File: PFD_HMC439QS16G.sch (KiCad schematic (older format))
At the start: 42 parts, among them J1 REF, J2 IN, J3 Out, J4 Supply, U1 HMC439QS16G, U2 LT3045EMSE, U3 LT3094EMSE, U4 ADA4896-2ARMZ

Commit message: Rev 1.1
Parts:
- added C20: 560p, Capacitor_SMD:C_0603_1608Metric, symbol Device:C_Small
- added C21, C22: 100n, Capacitor_SMD:C_0603_1608Metric, symbol Device:C_Small
- added C23: 33p, Capacitor_SMD:C_0603_1608Metric, symbol Device:C_Small
- added C24: 330p, Capacitor_SMD:C_0603_1608Metric, symbol Device:C_Small
- added H1, H2, H3, H4: MountingHole_Pad, MountingHole:MountingHole_4.3mm_M4_Pad_Via, symbol Mechanical:MountingHole_Pad
- added J5: JFET/Bias-T, Connector_Coaxial:SMA_Amphenol_901-144_Vertical, symbol Connector:Conn_Coaxial
- added JP1: Inverting, Jumper:SolderJumper-2_P1.3mm_Open_RoundedPad1.0x1.5mm, symbol Device:Jumper_NO_Small
- added JP2: Non-Inverting, Jumper:SolderJumper-2_P1.3mm_Open_RoundedPad1.0x1.5mm, symbol Device:Jumper_NO_Small
- added LOGO1: Logo_APQ, footprints:APQ-Logo, symbol Custom_logos:Logo_APQ
- added LOGO2: Logo_Open_Hardware_Small, Symbol:OSHW-Logo_5.7x6mm_SilkScreen, symbol Graphic:Logo_Open_Hardware_Small
- added LOGO3: Logo_ROHS, Symbol:RoHS-Logo_6mm_SilkScreen, symbol Custom_logos:Logo_ROHS
- added R16, R17, R18: 200, Resistor_SMD:R_0603_1608Metric, symbol Device:R_Small
- added R19: 51, Resistor_SMD:R_1210_3225Metric, symbol Device:R_Small
- added R20: 1.2k, Resistor_SMD:R_0603_1608Metric, symbol Device:R_Small
- added R21: 51, Resistor_SMD:R_0603_1608Metric, symbol Device:R_Small
- added RV1: 1k, Potentiometer_THT:Potentiometer_Vishay_43_Horizontal, symbol Device:R_POT_TRIM
- added U5: ADA4896-2ARMZ, footprints:MSOP-8_3x3mm_P0.65mm_mod, symbol Linear-Technology:ADA4896-2ARMZ
- C1, C2: footprint Capacitors_SMD:C_0402 -> Capacitor_SMD:C_0402_1005Metric
- C10, C15, C16, C17, C18, C19, C5, C6, C9: footprint Capacitors_SMD:C_0603 -> Capacitor_SMD:C_0603_1608Metric
- C11, C12, C3, C4: footprint Capacitors_SMD:C_1210 -> Capacitor_SMD:C_1210_3225Metric
- C13, C14: value 200p -> 33p; footprint Capacitors_SMD:C_0603 -> Capacitor_SMD:C_0603_1608Metric
- C7: footprint Capacitors_SMD:C_1206 -> Capacitor_SMD:C_1206_3216Metric
- C8: value 4.7u -> 0.47u; footprint Capacitors_SMD:C_1206 -> Capacitor_SMD:C_1206_3216Metric
- J1, J2: footprint Connectors:SMA_THT_Jack_Straight -> Connector_Coaxial:SMA_Amphenol_901-144_Vertical; symbol PFD_HMC439QS16G-rescue:CONN_01X02 -> Connector:Conn_Coaxial
- J3: value Out -> Error_Out; footprint Connectors:SMA_THT_Jack_Straight -> Connector_Coaxial:SMA_Amphenol_901-144_Vertical; symbol PFD_HMC439QS16G-rescue:CONN_01X02 -> Connector:Conn_Coaxial
- J4: footprint Pin_Headers:Pin_Header_Straight_1x03_Pitch2.54mm -> Connector_PinHeader_2.54mm:PinHeader_1x03_P2.54mm_Vertical; symbol PFD_HMC439QS16G-rescue:CONN_01X03 -> Connector_Generic:Conn_01x03
- R1, R10, R11, R12, R13, R14, R2, R3, R4, R5, R6, R7, R8, R9: footprint Resistors_SMD:R_0603 -> Resistor_SMD:R_0603_1608Metric
- R15: footprint Resistors_SMD:R_1210 -> Resistor_SMD:R_1210_3225Metric
- U1: footprint custom:QSOP-16_EP_3.9x4.9mm_Pitch0.635mm -> footprints:QSOP-16_3.9x4.9mm_P0.635mm_EP_2.3mmx1.75mm
- U2, U3: footprint Housings_SSOP:MSOP-12-1EP_3x4mm_Pitch0.65mm -> Package_SO:MSOP-12-1EP_3x4mm_P0.65mm_EP1.65x2.85mm
- U4: footprint Housings_SSOP:MSOP-8_3x3mm_Pitch0.65mm -> footprints:MSOP-8_3x3mm_P0.65mm_mod
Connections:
- wire segments 156 -> 210
- no-connect marks 0 -> 6
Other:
- note added: "Fixed Pi attenuator: 34 dB\n(reduce attenuation if \na larger 'gain' is required)"
- note added: "Non-inverting option:\nJP1: open, JP2: closed, R17: 200\n\nInverting option:\nJP1: closed, JP2: open, R17: DNF\n\n(Note, that U4B and U4A are inverting)"
- moved on the sheet: C1, C10, C11, C12, C13, C14, C15, C16, C17, C18, C19, C2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

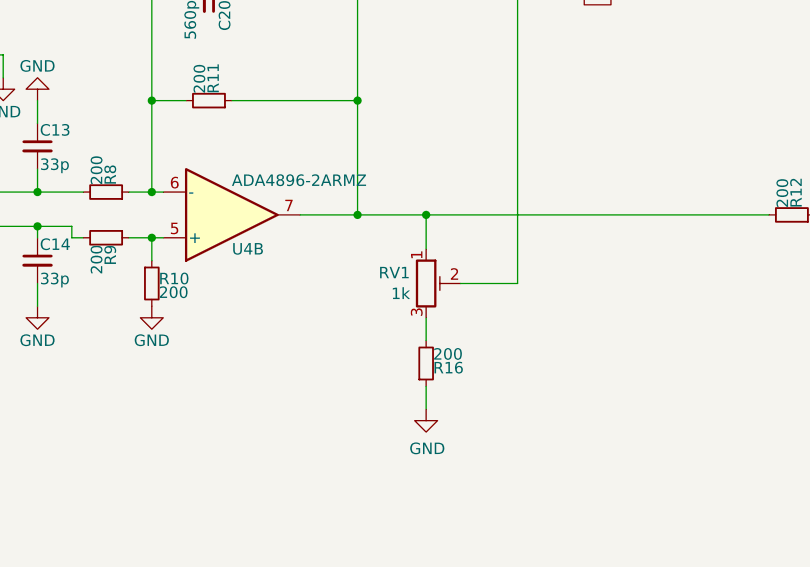
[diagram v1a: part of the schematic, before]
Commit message: Reverse Trimpot. Update gerber files
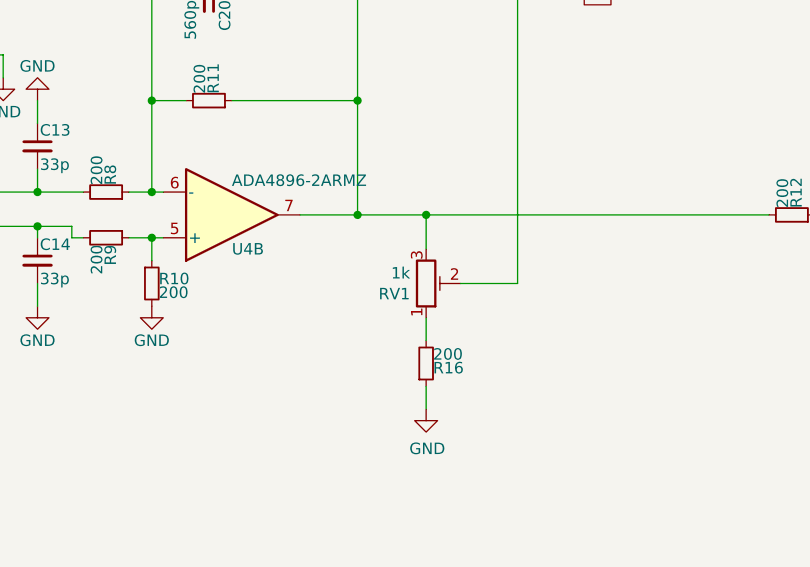
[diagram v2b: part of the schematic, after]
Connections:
- net at C20.1, R11.1, R12.2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: now also RV1.3; no longer RV1.1
- net at R16.2: now also RV1.1; no longer RV1.3
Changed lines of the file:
@@
 F 3 "~" H 6600 4050 50  0001 C CNN
 	1    6600 4050
-	1    0    0    -1
+	1    0    0    1
 $EndComp
 $Comp

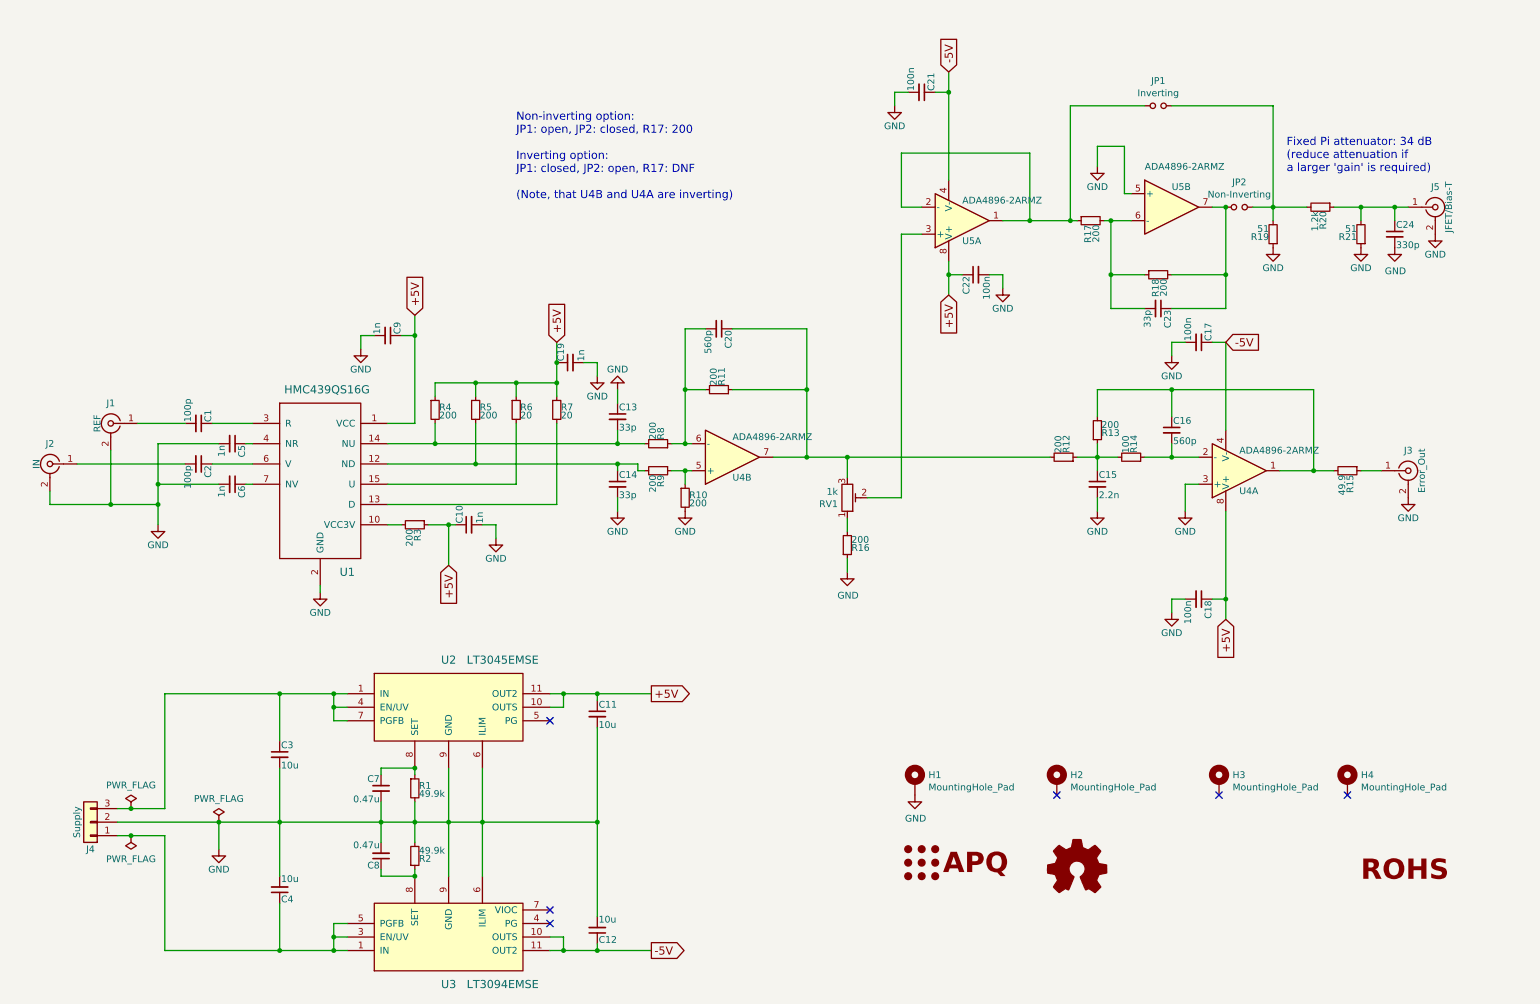
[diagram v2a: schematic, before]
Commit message: Rev. 1.2
-Divide input signal by 4 using HMC365
-Change board layout to standard eurocard
-Minor changes to 'Fast Out': Optional AC-coupling, optional gain
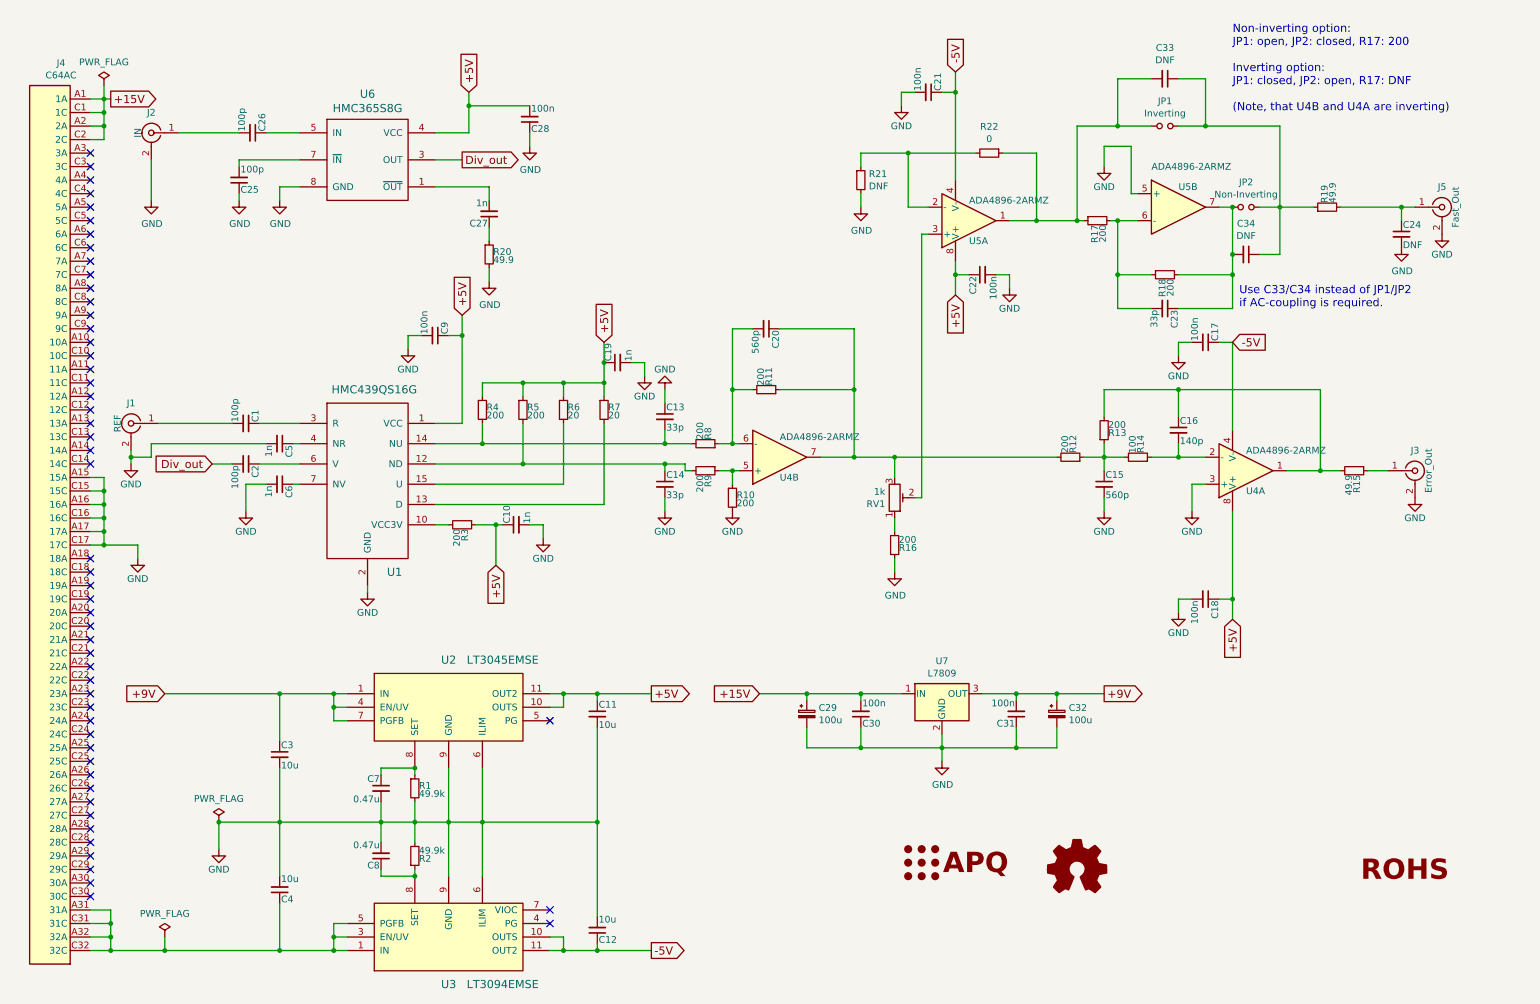
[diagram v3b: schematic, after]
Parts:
- removed H1, H2, H3, H4: MountingHole_Pad, MountingHole:MountingHole_4.3mm_M4_Pad_Via, symbol Mechanical:MountingHole_Pad
- removed J4: Supply, Connector_PinHeader_2.54mm:PinHeader_1x03_P2.54mm_Vertical, symbol Connector_Generic:Conn_01x03
- added C25, C26: 100p, Capacitor_SMD:C_0402_1005Metric, symbol Device:C_Small
- added C27: 1n, Capacitor_SMD:C_0603_1608Metric, symbol Device:C_Small
- added C28, C30, C31: 100n, Capacitor_SMD:C_0603_1608Metric, symbol Device:C_Small
- added C29, C32: 100u, Capacitor_THT:CP_Radial_D5.0mm_P2.50mm, symbol Device:CP_Small
- added C33, C34: DNF, Capacitor_THT:C_Rect_L7.2mm_W3.0mm_P5.00mm_FKS2_FKP2_MKS2_MKP2, symbol Device:C_Small
- added J4: C64AC, footprints:Socket_DIN41612-CaseC1-AC-Male-64Pin-2rows, symbol Connector:C64AC
- added R22: 0, Capacitor_SMD:C_0603_1608Metric, symbol Device:R_Small
- added U6: HMC365S8G, Package_SO:SOIC-8-1EP_3.9x4.9mm_P1.27mm_EP2.41x3.81mm, symbol Linear-Technology:HMC365S8G
- added U7: L7809, Package_TO_SOT_THT:TO-220-3_Vertical, symbol Regulator_Linear:L7809
- C15: value 2.2n -> 560p
- C16: value 560p -> 140p
- C24: value 330p -> DNF
- C9: value 1n -> 100n
- J3: footprint Connector_Coaxial:SMA_Amphenol_901-144_Vertical -> Connector_Coaxial:BNC_Amphenol_B6252HB-NPP3G-50_Horizontal
- J5: value JFET/Bias-T -> Fast_Out; footprint Connector_Coaxial:SMA_Amphenol_901-144_Vertical -> Connector_Coaxial:BNC_Amphenol_B6252HB-NPP3G-50_Horizontal
- R19: value 51 -> 49.9
- R20: value 1.2k -> 49.9
- R21: value 51 -> DNF; footprint Resistor_SMD:R_0603_1608Metric -> Capacitor_SMD:C_0603_1608Metric
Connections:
- net +5V: now also C28.2, U6.4 (VCC)
- net GND: now also R20.2, R21.2, C25.1, C28.1, C29.2, C30.1, C31.1, C32.2, J4.A15 (15A), J4.A16 (16A), J4.A17 (17A), J4.C15 (15C), J4.C16 (16C), J4.C17 (17C), U6.8 (GND), U6.9 (GND), U7.2 (GND); no longer R19.1, R21.1
- net IN: now also J4.A31 (31A), J4.A32 (32A), J4.C31 (31C), J4.C32 (32C)
- net IN2: now also C31.2, C32.1, U7.3 (OUT)
- net at J2.1 (In): now also C26.2; no longer C2.2
- net at C24.1, J5.1 (In): now also R19.2; no longer R20.1, R21.2
- net at JP1.2, JP2.2: now also R19.1, C33.1, C34.1; no longer R19.2, R20.2
- net at JP1.1, R17.1, U5.1: now also C33.2, R22.1; no longer U5.2 (-)
- net at C23.1, JP2.1, R18.2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: now also C34.2
- new net: R21.1, R22.2, U5.2 (-)
- new net: C27.2, U6.1 (~OUT~)
- new net: C26.1, U6.5 (IN)
- new net: C25.2, U6.7 (~IN~)
- new net: C27.1, R20.1
- new net +15V: C29.1, C30.2, J4.A1 (1A), J4.A2 (2A), J4.C1 (1C), J4.C2 (2C), U7.1 (IN)
- new net Div_out: C2.2, U6.3 (OUT)
- no-connect marks 6 -> 53
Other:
- note added: "Use C33/C34 instead of JP1/JP2\nif AC-coupling is required."
- note removed: "Fixed Pi attenuator: 34 dB\n(reduce attenuation if \na larger 'gain' is required)"
- moved on the sheet: C1, C10, C13, C14, C15, C16, C17, C18, C19, C2, C20, C21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

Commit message: Add gain of 2 and increase bandwidth at U4B
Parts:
- C20: value 560p -> 15p
- R10, R11: value 200 -> 380
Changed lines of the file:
@@
 P 5750 4050
 F 0 "R10" H 5780 4070 50  0000 L CNN
-F 1 "200" H 5780 4010 50  0000 L CNN
+F 1 "380" H 5780 4010 50  0000 L CNN
 F 2 "Resistor_SMD:R_0603_1608Metric" H 5750 4050 50  0001 C CNN
 F 3 "" H 5750 4050 50  0001 C CNN
@@
 P 6000 3250
 F 0 "R11" H 6030 3270 50  0000 L CNN
-F 1 "200" H 6030 3210 50  0000 L CNN
+F 1 "380" H 6030 3210 50  0000 L CNN
 F 2 "Resistor_SMD:R_0603_1608Metric" H 6000 3250 50  0001 C CNN
 F 3 "" H 6000 3250 50  0001 C CNN
@@
 P 6000 2800
 F 0 "C20" H 6010 2870 50  0000 L CNN
-F 1 "560p" H 6010 2720 50  0000 L CNN
+F 1 "15p" H 6010 2720 50  0000 L CNN
 F 2 "Capacitor_SMD:C_0603_1608Metric" H 6000 2800 50  0001 C CNN
 F 3 "" H 6000 2800 50  0001 C CNN

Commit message: First draft: fast PD regulator
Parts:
- removed C21, C22: 100n, Capacitor_SMD:C_0603_1608Metric, symbol Device:C_Small
- removed C23: 33p, Capacitor_SMD:C_0603_1608Metric, symbol Device:C_Small
- removed C24: DNF, Capacitor_SMD:C_0603_1608Metric, symbol Device:C_Small
- removed C33, C34: DNF, Capacitor_THT:C_Rect_L7.2mm_W3.0mm_P5.00mm_FKS2_FKP2_MKS2_MKP2, symbol Device:C_Small
- removed J5: Fast_Out, Connector_Coaxial:BNC_Amphenol_B6252HB-NPP3G-50_Horizontal, symbol Connector:Conn_Coaxial
- removed JP1: Inverting, Jumper:SolderJumper-2_P1.3mm_Open_RoundedPad1.0x1.5mm, symbol Device:Jumper_NO_Small
- removed JP2: Non-Inverting, Jumper:SolderJumper-2_P1.3mm_Open_RoundedPad1.0x1.5mm, symbol Device:Jumper_NO_Small
- removed R16, R17, R18: 200, Resistor_SMD:R_0603_1608Metric, symbol Device:R_Small
- removed R19: 49.9, Resistor_SMD:R_1210_3225Metric, symbol Device:R_Small
- removed R21: DNF, Capacitor_SMD:C_0603_1608Metric, symbol Device:R_Small
- removed R22: 0, Capacitor_SMD:C_0603_1608Metric, symbol Device:R_Small
- removed RV1: 1k, Potentiometer_THT:Potentiometer_Vishay_43_Horizontal, symbol Device:R_POT_TRIM
- removed U5: ADA4896-2ARMZ, footprints:MSOP-8_3x3mm_P0.65mm_mod, symbol Linear-Technology:ADA4896-2ARMZ
- added C21: 100u, Capacitor_THT:CP_Radial_D5.0mm_P2.50mm, symbol Device:CP_Small
- added D1, D2: SMB, Diode_SMD:D_SMB, symbol Device:D_TVS
- C13, C14: value 33p -> 15p
- U7: value L7809 -> L7808; symbol Regulator_Linear:L7809 -> Regulator_Linear:L7808
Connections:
- net +15V: now also D1.1 (A1)
- net GND: now also J4.A18 (18A), J4.C18 (18C), C21.1, D1.2 (A2), D2.1 (A1)
- net IN: now also C21.2, D2.2 (A2)
- net Fast PD regulator/error_sig: now reaches C20.1, R11.1, R12.2, U4.7
- no-connect marks 53 -> 51
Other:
- note removed: "Non-inverting option:\nJP1: open, JP2: closed, R17: 200\n\nInverting option:\nJP1: closed, JP2: open, R17: DNF\n\n(Note, that U4B and U4A are inverting)"
- note removed: "Use C33/C34 instead of JP1/JP2\nif AC-coupling is required."
- moved on the sheet: C15, C16, C17, C18, C25, C26, C27, C28, J2, J3, R12, R13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

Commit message: Fast PD second draft
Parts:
- J1, J2: footprint Connector_Coaxial:SMA_Amphenol_901-144_Vertical -> Connector_Coaxial:SMA_Amphenol_132289_EdgeMount
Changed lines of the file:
@@
 F 0 "J1" H 1300 3650 50  0000 C CNN
 F 1 "REF" V 1400 3500 50  0000 C CNN
-F 2 "Connector_Coaxial:SMA_Amphenol_901-144_Vertical" H 1300 3500 50  0001 C CNN
+F 2 "Connector_Coaxial:SMA_Amphenol_132289_EdgeMount" H 1300 3500 50  0001 C CNN
 F 3 "" H 1300 3500 50  0001 C CNN
 	1    1300 3500
@@
 F 0 "J2" H 2850 1250 50  0000 C CNN
 F 1 "IN" V 2950 1100 50  0000 C CNN
-F 2 "Connector_Coaxial:SMA_Amphenol_901-144_Vertical" H 2850 1100 50  0001 C CNN
+F 2 "Connector_Coaxial:SMA_Amphenol_132289_EdgeMount" H 2850 1100 50  0001 C CNN
 F 3 "" H 2850 1100 50  0001 C CNN
 	1    2850 1100
